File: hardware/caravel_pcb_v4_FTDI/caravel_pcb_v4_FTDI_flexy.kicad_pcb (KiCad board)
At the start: 2 copper layers, 76.2 x 73.8 mm, 65 parts, among them J1 USB_B_Micro - 10118193-0001LF, J10 Conn_01x27_Female, J11 Conn_01x20_Female, J2 Conn_01x02_Female, J3 Conn_01x02_Male, J4 Conn_01x04_Female, J5 Conn_01x02_Male, J6 Conn_01x02_Male, J7 Conn_01x06_Female, J8 Conn_01x02_Male, J9 Conn_01x02_Male, SW1 SW_Push - SKQGADE010, T1 Logo, T2 Logo, U1 FT232H, U2 SN74LVC1G125DCKR, U3 SN74LVC1G125DCKR, U4 AZ1117CH-1.8TRG1, U5 AZ1117-3.3, U6 caravel_breakout, U7 W25Q32FVSS, X1 DSC6001_10MHZ, Y1 CSTNE12M0GH5L000R0

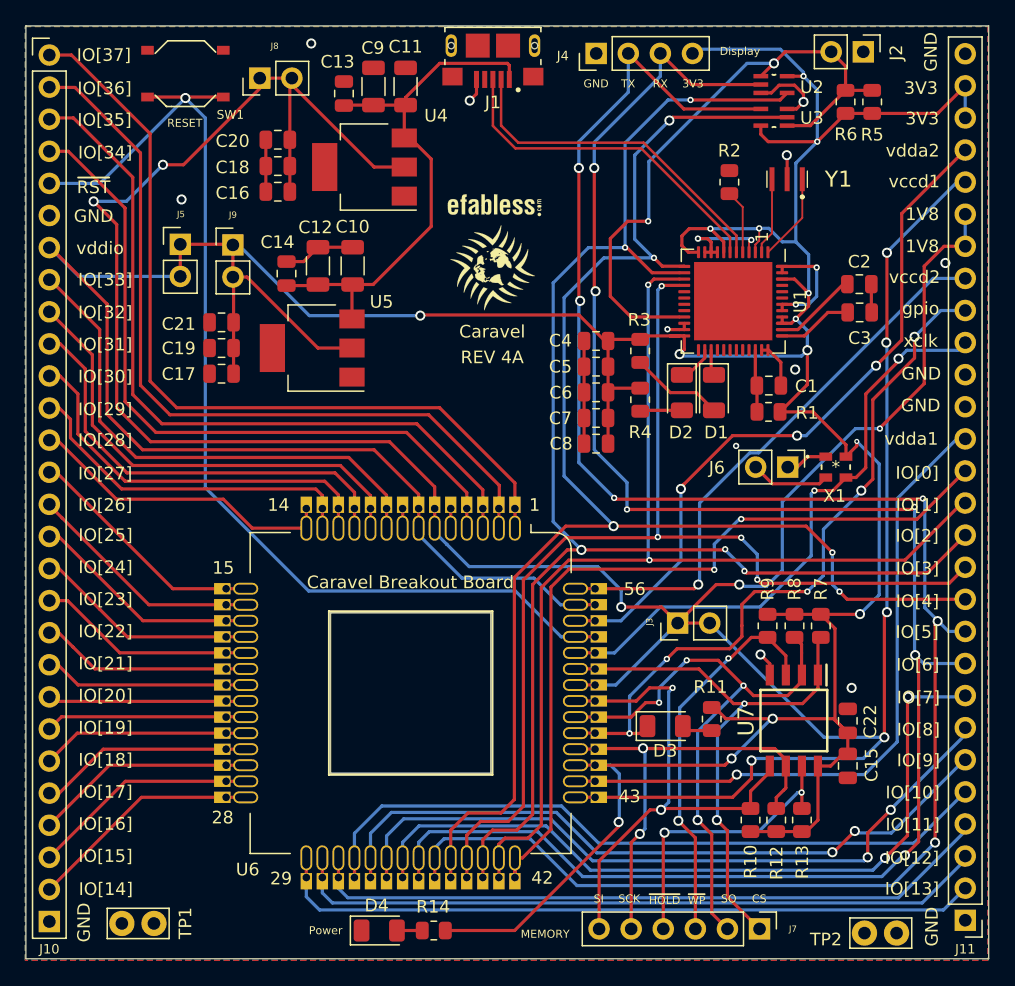
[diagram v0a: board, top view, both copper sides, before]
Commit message: update caravel FTDI mainboard V4 (Rev 4B)
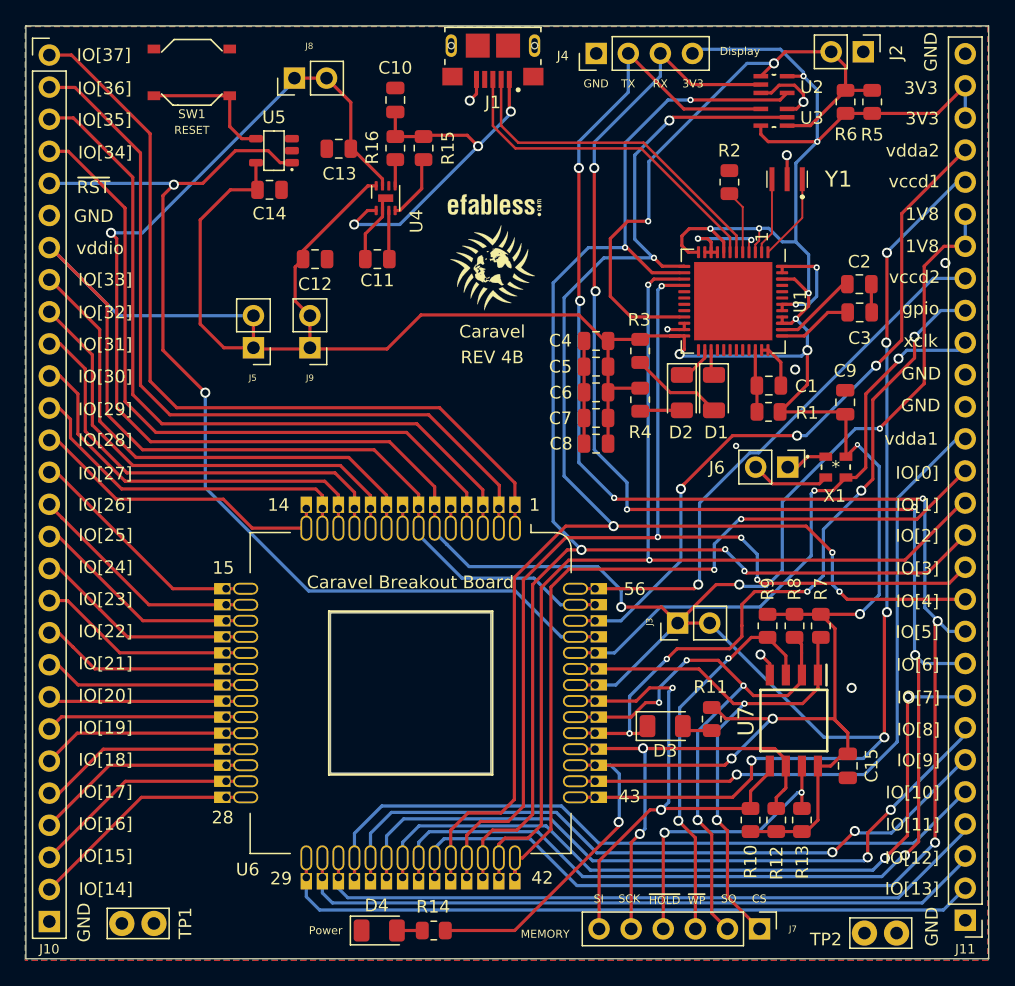
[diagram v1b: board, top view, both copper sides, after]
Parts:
- removed C16, C17: 22uf - CC0805MKX5R5BB226, Capacitor_SMD:C_0805_2012Metric
- removed C18, C19: 10uf - CC0805KKX5R8BB106, Capacitor_SMD:C_0805_2012Metric
- removed C20, C21: 1uf, Capacitor_SMD:C_0805_2012Metric
- removed C22: 0.1uf - CC0805KRX7R9BB104, Capacitor_SMD:C_0805_2012Metric
- added R15: 10k, Resistor_SMD:R_0805_2012Metric, F.Cu at (131.5, 68.4)
- added R16: 10k, Resistor_SMD:R_0805_2012Metric, F.Cu at (129.2, 68.4)
- C10: value 100uf - GRM31CR60J107ME39L -> 10uf - CC0805KKX5R8BB106; footprint Capacitor_SMD:C_1206_3216Metric -> Capacitor_SMD:C_0805_2012Metric
- C11, C9: value 100uf - GRM31CR60J107ME39L -> 0.1uf - CC0805KRX7R9BB104; footprint Capacitor_SMD:C_1206_3216Metric -> Capacitor_SMD:C_0805_2012Metric
- C12: value 100uf - GRM31CR60J107ME39L -> 2.2uf - CC0805MKX5R6BB225; footprint Capacitor_SMD:C_1206_3216Metric -> Capacitor_SMD:C_0805_2012Metric
- C13: value 10uf - CC0805KKX5R8BB106 -> 2.2uf - CC0805MKX5R6BB225
- C14: value 10uf - CC0805KKX5R8BB106 -> 0.1uf - CC0805KRX7R9BB104
- U4: value AZ1117CH-1.8TRG1 -> MIC5350-SGYMT-TR; footprint Package_TO_SOT_SMD:SOT-223 -> Package_DFN_QFN:DFN-8-1EP_2x2mm_P0.5mm_EP0.6x1.2mm
- U5: value AZ1117-3.3 -> MCP1319MT-29LE-OT; footprint Package_TO_SOT_SMD:SOT-223 -> Caravel_Board:PoR_5_SOT23
- moved C9 44.9 mm to (164.8, 88.5)
- moved U5 15.9 mm to (119.6, 68.6)
- moved C11 13.8 mm to (127.8, 77.2), turned to 180 degrees
- moved C10 13.6 mm to (129.2, 64.6)
- moved J9 10.2 mm to (122.5, 84.2), turned to 180 degrees
- moved J5 10.0 mm to (118.0, 84.2), turned to 180 degrees
- moved C14 6.76 mm to (119.3, 71.7), turned to 180 degrees
- moved C13 4.39 mm to (124.8, 68.5), turned to 0 degrees
- moved U4 2.98 mm to (128.5, 72.4), turned to 90 degrees
- moved J8 2.74 mm to (121.3, 62.9)
- moved C12 0.58 mm to (122.9, 77.2), turned to 180 degrees
- moved SW1 0.52 mm to (113.1, 62.4)
- turned C15 to -90 degrees
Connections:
- C11 pad 1: GND -> Net-(C11-Pad1)
- C11 pad 2: +5V -> GND
- C12 pad 2: +5V -> vdda
- C13 pad 2: +5V -> vccd
- C14 pad 2: +5V -> vdda
- C15 pad 1: GND -> vdda
- C15 pad 2: vdda -> GND
- C9 pad 2: +5V -> vdda
- SW1 pad 1: ~{RST} -> ~{MR}
- U4 pad 1: GND -> +5V
- U4 pad 2: vccd -> GND
- U4 pad 3: +5V -> Net-(C11-Pad1)
- U4 pad 4: (no net) -> Net-(R15-Pad1)
- U5 pad 1: GND -> ~{RST}
- U5 pad 2: vdda -> GND
- U5 pad 3: +5V -> unconnected-(U5-Pad3)
- U5 pad 4: (no net) -> ~{MR}
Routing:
- net vdda: track 356.4 -> 373.0 mm, vias 14 -> 13
- net +5V: track 43.1 -> 29.7 mm, vias 0 -> 3
- net vccd: track 263.7 -> 251.9 mm, vias 10 -> 9
- net ~{MR}: track 0.00 -> 10.8 mm
- net Net-(R15-Pad1): track 0.00 -> 5.18 mm
- net ~{RST}: track 86.9 -> 82.2 mm, vias 1 -> 2
- net GND: track 64.3 -> 59.9 mm, vias 15 -> 13
- net Net-(C11-Pad1): track 0.00 -> 3.80 mm
- net Net-(R16-Pad1): track 0.00 -> 2.16 mm
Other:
- board text added: "REV 4B"
- board text removed: "REV 4A"

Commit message: update caravel FTDI mainboard V4 (Rev 4B) to support different LDO devices with the same footprint
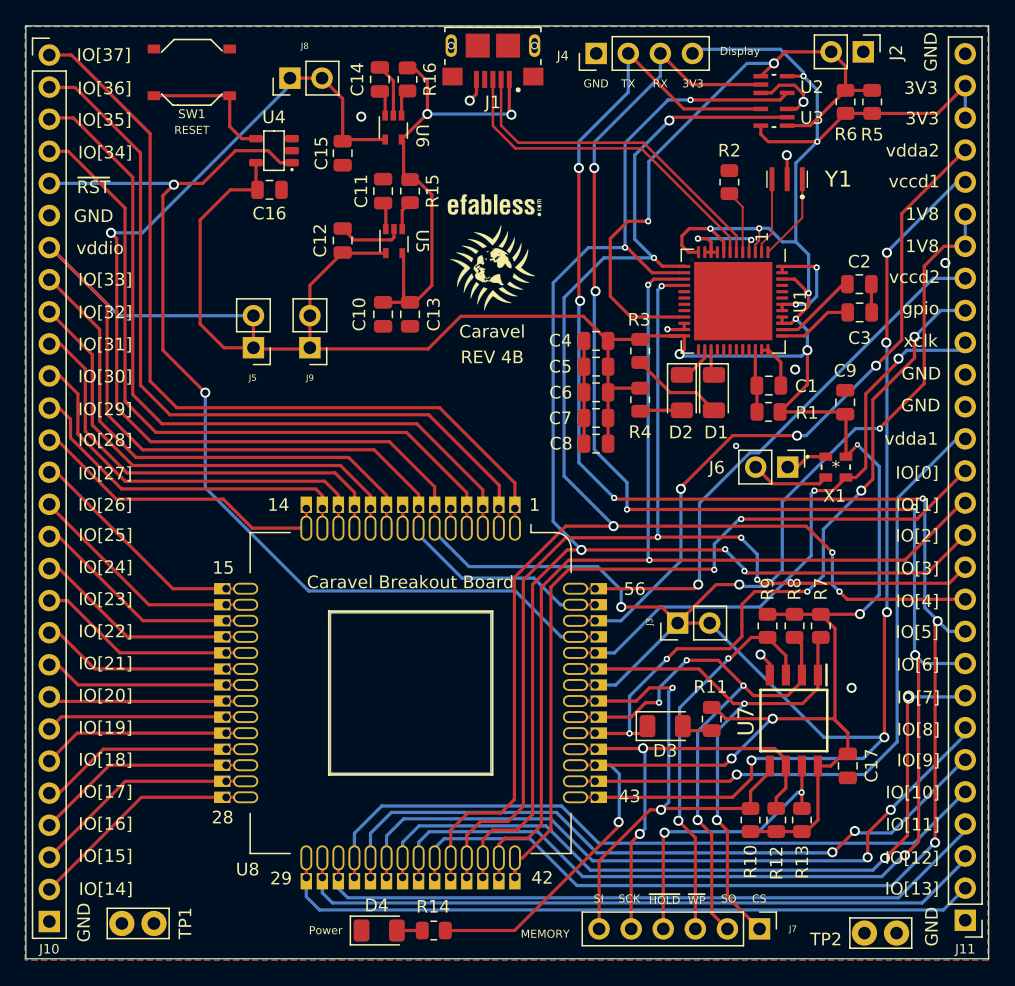
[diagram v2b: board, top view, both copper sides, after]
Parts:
- removed the U4 at (128.5, 72.4)
- added C14: 0.01uf - CC0805KRX7R9BB103, Capacitor_SMD:C_0805_2012Metric, F.Cu at (128.0, 63.0)
- added C15: 10uf - CC0805KKX5R8BB106, Capacitor_SMD:C_0805_2012Metric, F.Cu at (125.1, 68.8)
- added U5: TAR5SxxU_SOT353F, Caravel_Board:SOT-353F, F.Cu at (129.1, 75.8)
- added U6: TAR5SxxU_SOT353F, Caravel_Board:SOT-353F, F.Cu at (129.1, 66.8)
- C10: value 10uf - CC0805KKX5R8BB106 -> 1uf - CC0805KKX5R8BB105
- C11: value 0.1uf - CC0805KRX7R9BB104 -> 0.01uf - CC0805KRX7R9BB103
- C12: value 2.2uf - CC0805MKX5R6BB225 -> 10uf - CC0805KKX5R8BB106
- C13: value 2.2uf - CC0805MKX5R6BB225 -> 1uf - CC0805KKX5R8BB105
- moved C10 17.0 mm to (128.3, 81.6), turned to 90 degrees
- moved C13 14.3 mm to (130.4, 81.6), turned to 90 degrees
- moved R16 5.52 mm to (130.2, 63.0)
- moved C11 5.40 mm to (128.3, 71.8), turned to 90 degrees
- moved R15 3.57 mm to (130.4, 71.8)
- moved C12 2.63 mm to (125.1, 75.7), turned to -90 degrees
- moved J8 0.36 mm to (120.9, 62.9)
- renumbered C14 to C16, C15 to C17, U5 to U4, U6 to U8
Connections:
- C13 pad 2: vccd -> +5V
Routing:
- net +5V: track 29.7 -> 38.4 mm, vias 3 -> 2
- net vdda: track 373.0 -> 368.6 mm
- net GND: track 59.9 -> 63.8 mm, vias 13 -> 14
- net Net-(R15-Pad1): track 5.18 -> 2.36 mm
- net Net-(C14-Pad1): track 0.00 -> 2.08 mm
- net Net-(C11-Pad1): track 3.80 -> 2.15 mm
- net vccd: track 251.9 -> 250.6 mm
